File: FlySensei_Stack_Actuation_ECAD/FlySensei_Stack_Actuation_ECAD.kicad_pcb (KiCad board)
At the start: 4 copper layers, 90 x 65 mm, 122 parts, among them J1 Conn_02x20_Odd_Even_Male, J2 Conn_02x20_Odd_Even_Female, J3 Conn_02x20_Odd_Even_Male, J4 Conn_02x20_Odd_Even_Female, J5 JST_PH_SM2, M0 JST_SH_SM02, M1 JST_SH_SM02, M2 JST_SH_SM02, M3 JST_SH_SM02, SW1 SW_SPDT, SW2 SW_SPDT, U1 PCA9685BS, U10 TS5A3159ADCKR, U2 DRV8835DSSR, U3 DRV8835DSSR, U4 DRV8835DSSR, U5 DRV8835DSSR, U6 MPM3610, U7 MPM3610, U8 MAX17048G+T10, U9 TS5A3159ADCKR

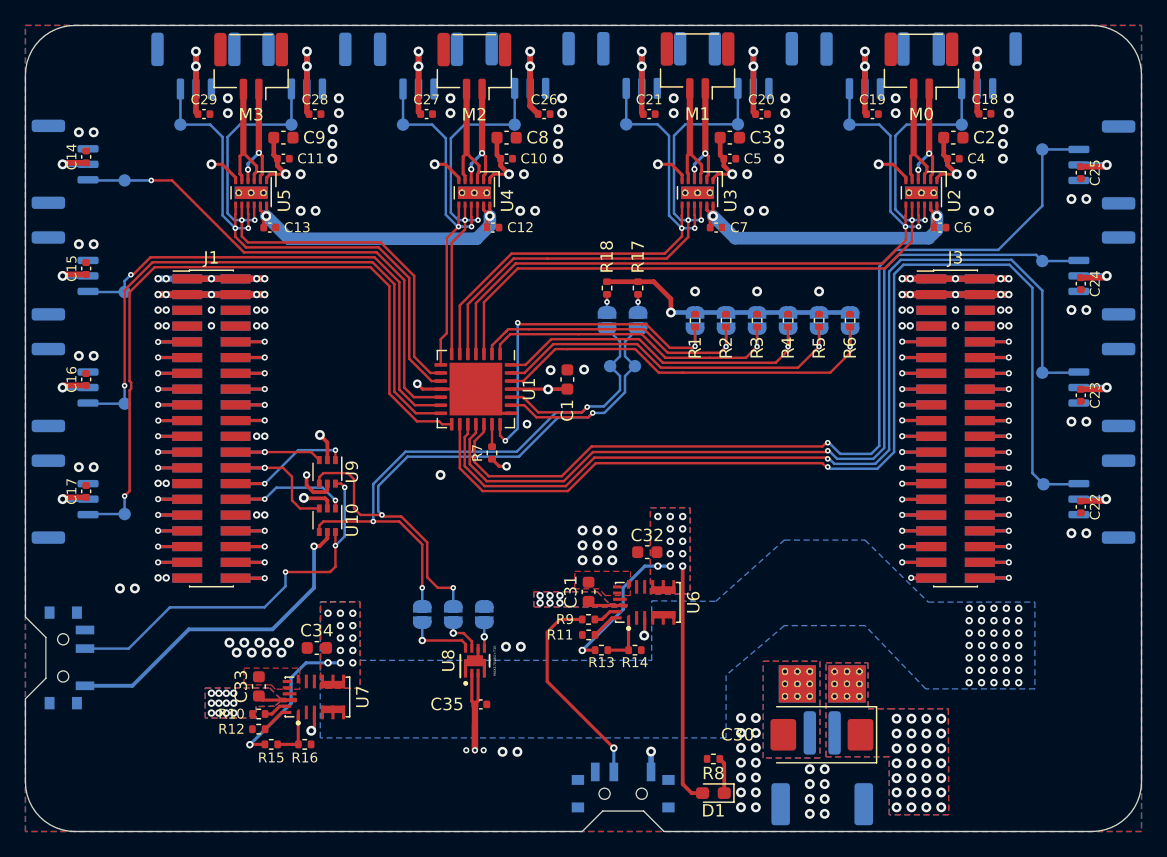
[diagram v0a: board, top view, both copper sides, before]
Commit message: Change PWM generation IC package to TSSOP due to availibility
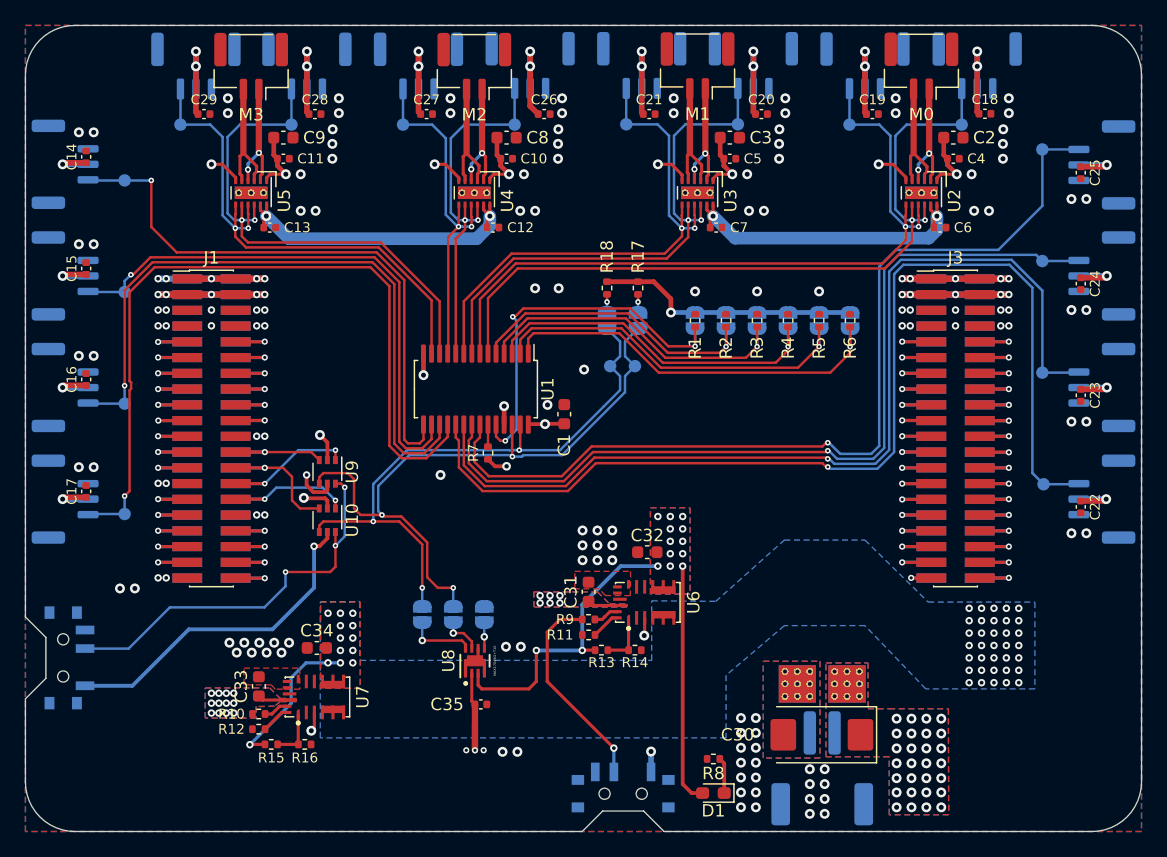
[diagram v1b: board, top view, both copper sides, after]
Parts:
- U1: value PCA9685BS -> PCA9685PW; footprint Package_DFN_QFN:QFN-28-1EP_6x6mm_P0.65mm_EP4.25x4.25mm -> Package_SO:TSSOP-28_4.4x9.7mm_P0.65mm
- U8: value MAX17048G+T10 -> MAX17049G+T10
- moved C1 2.81 mm to (133.4, 96.3)
- moved R7 0.33 mm to (127.3, 99.5)
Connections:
- U1 pad 1: /PWM Generator/I2C_A3 -> /PWM Generator/I2C_A0
- U1 pad 10: /Actuation Connectors/PWM7 -> /Actuation Connectors/PWM4
- U1 pad 11: GND -> /Actuation Connectors/PWM5
- U1 pad 12: /Actuation Connectors/PWM8 -> /Actuation Connectors/PWM6
- U1 pad 13: /Actuation Connectors/PWM9 -> /Actuation Connectors/PWM7
- U1 pad 14: /Actuation Connectors/PWM10 -> GND
- U1 pad 15: /Actuation Connectors/PWM11 -> /Actuation Connectors/PWM8
- U1 pad 16: /Actuation Connectors/PWM12 -> /Actuation Connectors/PWM9
- U1 pad 17: /Actuation Connectors/PWM13 -> /Actuation Connectors/PWM10
- U1 pad 18: /Actuation Connectors/PWM14 -> /Actuation Connectors/PWM11
- U1 pad 19: /Actuation Connectors/PWM15 -> /Actuation Connectors/PWM12
- U1 pad 2: /PWM Generator/I2C_A4 -> /PWM Generator/I2C_A1
- U1 pad 20: Net-(R7-Pad2) -> /Actuation Connectors/PWM13
- U1 pad 21: /PWM Generator/I2C_A5 -> /Actuation Connectors/PWM14
- U1 pad 22: GND -> /Actuation Connectors/PWM15
- U1 pad 23: /I2C Mux/I2C_SCL -> Net-(R7-Pad2)
- U1 pad 24: /I2C Mux/I2C_SDA -> /PWM Generator/I2C_A5
- U1 pad 25: +3V3 -> GND
- U1 pad 26: /PWM Generator/I2C_A0 -> /I2C Mux/I2C_SCL
- U1 pad 27: /PWM Generator/I2C_A1 -> /I2C Mux/I2C_SDA
- U1 pad 28: /PWM Generator/I2C_A2 -> +3V3
- U1 pad 3: /Actuation Connectors/PWM0 -> /PWM Generator/I2C_A2
- U1 pad 4: /Actuation Connectors/PWM1 -> /PWM Generator/I2C_A3
- U1 pad 5: /Actuation Connectors/PWM2 -> /PWM Generator/I2C_A4
- U1 pad 6: /Actuation Connectors/PWM3 -> /Actuation Connectors/PWM0
- U1 pad 7: /Actuation Connectors/PWM4 -> /Actuation Connectors/PWM1
- U1 pad 8: /Actuation Connectors/PWM5 -> /Actuation Connectors/PWM2
- U1 pad 9: /Actuation Connectors/PWM6 -> /Actuation Connectors/PWM3
- U8 pad 3: +BATT -> +3V3
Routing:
- net +3V3: track 158.1 -> 169.1 mm, vias 23 -> 24
- net /Actuation Connectors/PWM8: track 40.8 -> 46.9 mm
- net GND: track 32.2 -> 26.9 mm, vias 141 -> 143
- net /Actuation Connectors/PWM10: track 48.7 -> 54.0 mm
- net /Actuation Connectors/PWM11: track 58.3 -> 63.2 mm
- net /I2C Mux/I2C_SDA: track 53.7 -> 48.9 mm
- net /Actuation Connectors/PWM9: track 40.2 -> 44.8 mm
- net /I2C Mux/I2C_SCL: track 58.7 -> 54.2 mm
- net /Actuation Connectors/PWM7: track 45.2 -> 42.3 mm
- net +BATT: track 170.9 -> 168.2 mm
- net /Actuation Connectors/PWM6: track 45.3 -> 43.2 mm
- net /PWM Generator/I2C_A5: track 29.6 -> 31.6 mm
- net /PWM Generator/I2C_A2: track 27.8 -> 29.0 mm
- net /Actuation Connectors/PWM5: track 30.7 -> 29.6 mm
- net /PWM Generator/I2C_A3: track 26.0 -> 26.9 mm
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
